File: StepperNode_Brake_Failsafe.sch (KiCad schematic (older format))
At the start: 8 parts, among them P6 TE_640456-8, U13 74LVC1G32GW,125, U14 74LVC1G32GW,125, U15 NUD3124LT1G

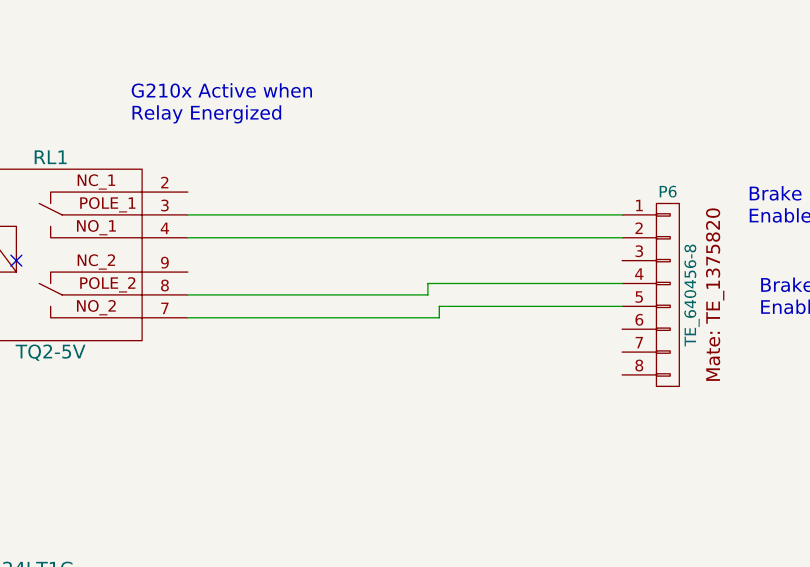
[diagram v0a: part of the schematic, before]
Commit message: Fix most ERC warnings (non-connected pins, etc)
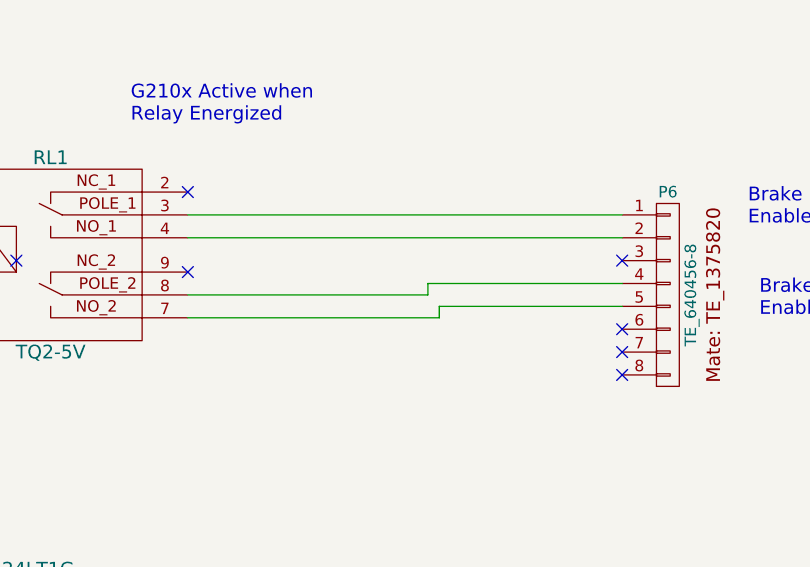
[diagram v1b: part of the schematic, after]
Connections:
- no-connect marks 1 -> 7
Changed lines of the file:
@@
 	9050 4550 9050 4900
 $Comp
-L GNDD #PWR100
+L GNDD #PWR0101
 U 1 1 575D769D
 P 9050 5900
-F 0 "#PWR100" H 9050 5650 50  0001 C CNN
+F 0 "#PWR0101" H 9050 5650 50  0001 C CNN
 F 1 "GNDD" H 9050 5750 50  0000 C CNN
 F 2 "" H 9050 5900 50  0000 C CNN
@@
 	4150 5600 5000 5600
 $Comp
-L GNDD #PWR94
+L GNDD #PWR0102
 U 1 1 575DA88C
 P 5500 6000
-F 0 "#PWR94" H 5500 5750 50  0001 C CNN
+F 0 "#PWR0102" H 5500 5750 50  0001 C CNN
 F 1 "GNDD" H 5500 5850 50  0000 C CNN
 F 2 "" H 5500 6000 50  0000 C CNN
@@
 Output is high when either\nInterlock is on
 $Comp
-L GNDD #PWR96
+L GNDD #PWR0103
 U 1 1 575DAC78
 P 7200 5900
-F 0 "#PWR96" H 7200 5650 50  0001 C CNN
+F 0 "#PWR0103" H 7200 5650 50  0001 C CNN
 F 1 "GNDD" H 7200 5750 50  0000 C CNN
 F 2 "" H 7200 5900 50  0000 C CNN
@@
 $EndComp
 $Comp
-L +3V3_A #PWR93
+L +3V3_A #PWR0104
 U 1 1 575A85D8
 P 5500 5050
-F 0 "#PWR93" H 5500 4900 50  0001 C CNN
+F 0 "#PWR0104" H 5500 4900 50  0001 C CNN
 F 1 "+3V3_A" H 5500 5190 50  0000 C CNN
 F 2 "" H 5500 5050 60  0000 C CNN
@@
 $EndComp
 $Comp
-L +3V3_A #PWR95
+L +3V3_A #PWR0105
 U 1 1 575A85F8
 P 7200 4950
-F 0 "#PWR95" H 7200 4800 50  0001 C CNN
+F 0 "#PWR0105" H 7200 4800 50  0001 C CNN
 F 1 "+3V3_A" H 7200 5090 50  0000 C CNN
 F 2 "" H 7200 4950 60  0000 C CNN
@@
 $EndComp
 $Comp
-L GNDD #PWR92
+L GNDD #PWR0106
 U 1 1 575A86D0
 P 5450 7150
-F 0 "#PWR92" H 5450 6900 50  0001 C CNN
+F 0 "#PWR0106" H 5450 6900 50  0001 C CNN
 F 1 "GNDD" H 5450 7000 50  0000 C CNN
 F 2 "" H 5450 7150 50  0000 C CNN
@@
 $EndComp
 $Comp
-L +3V3_A #PWR91
+L +3V3_A #PWR0107
 U 1 1 575A86E0
 P 5450 6850
-F 0 "#PWR91" H 5450 6700 50  0001 C CNN
+F 0 "#PWR0107" H 5450 6700 50  0001 C CNN
 F 1 "+3V3_A" H 5450 6990 50  0000 C CNN
 F 2 "" H 5450 6850 60  0000 C CNN
@@
 $EndComp
 $Comp
-L GNDD #PWR98
+L GNDD #PWR0108
 U 1 1 575A8920
 P 7200 7200
-F 0 "#PWR98" H 7200 6950 50  0001 C CNN
+F 0 "#PWR0108" H 7200 6950 50  0001 C CNN
 F 1 "GNDD" H 7200 7050 50  0000 C CNN
 F 2 "" H 7200 7200 50  0000 C CNN
@@
 $EndComp
 $Comp
-L +3V3_A #PWR97
+L +3V3_A #PWR0109
 U 1 1 575A8926
 P 7200 6900
-F 0 "#PWR97" H 7200 6750 50  0001 C CNN
+F 0 "#PWR0109" H 7200 6750 50  0001 C CNN
 F 1 "+3V3_A" H 7200 7040 50  0000 C CNN
 F 2 "" H 7200 6900 60  0000 C CNN
@@
 $EndComp
 $Comp
-L +5V_A #PWR99
+L +5V_A #PWR0110
 U 1 1 5765374C
 P 8750 4150
-F 0 "#PWR99" H 8750 4000 50  0001 C CNN
+F 0 "#PWR0110" H 8750 4000 50  0001 C CNN
 F 1 "+5V_A" H 8750 4290 50  0000 C CNN
 F 2 "" H 8750 4150 60  0000 C CNN
@@
 Text Notes 2850 3300 0    60   ~ 0
 The purpose of this function is to ensure that if the WDT_GOOD signal \ngoes low the drive controllers do not drop out if the interlock is enabled.\n
+NoConn ~ 12150 4400
+NoConn ~ 12150 4700
+NoConn ~ 12150 4800
+NoConn ~ 12150 4900
+NoConn ~ 10250 4100
+NoConn ~ 10250 4450
 $EndSCHEMATC
